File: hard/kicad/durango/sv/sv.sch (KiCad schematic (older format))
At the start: 22 parts, among them U1 74HCT02, U10 74HC245, U11 74HCT374, U12 74HC245, U13 74HC257, U15 74HC257, U16 74HC257, U17 74HC257, U18 74HC257, U2 74HCT4040, U3 74HC21, U4 74HCT4040, U5 74HC21, U6 74HCT85, U7 74HCT85, U8 74HCT85, U9 74HC175, X1 ACO-18.432MHz

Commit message: trying buses on durango kicad schematics
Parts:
- added U14: 6264, Package_DIP:DIP-28_W15.24mm, symbol Memory_RAM:6264
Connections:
- net VD7: now reaches U12.11 (B7)
- net VD7: now also U11.18 (D7), U14.19 (D7)
- net VD6: now reaches U12.12 (B6)
- net VD6: now also U11.17 (D6), U14.18 (D6)
- net VD5: now reaches U12.13 (B5)
- net VD5: now also U11.14 (D5), U14.17 (D5)
- net VD4: now reaches U12.14 (B4)
- net VD4: now also U11.13 (D4), U14.16 (D4)
- net VD3: now reaches U12.15 (B3)
- net VD3: now also U11.8 (D3), U14.15 (D3)
- net VD2: now reaches U12.16 (B2)
- net VD2: now also U11.7 (D2), U14.13 (D2)
- net VD1: now reaches U12.17 (B1)
- net VD1: now also U11.4 (D1), U14.12 (D1)
- net VD0: now reaches U12.18 (B0)
- net VD0: now also U11.3 (D0), U14.11 (D0)
- net \SEL renamed ~SEL
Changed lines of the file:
@@
 Connection ~ 800  7700
 Text GLabel 700  7700 0    50   Input ~ 0
-\SEL
+~SEL
 Wire Wire Line
 	7150 3500 7200 3500
@@
 Wire Wire Line
 	10100 5500 10050 5500
+$Comp
+L Memory_RAM:6264 U14
+U 1 1 606818EE
+P 6600 5400
+F 0 "U14" H 6600 6581 50  0000 C CNN
+F 1 "6264" H 6600 6490 50  0000 C CNN
+F 2 "Package_DIP:DIP-28_W15.24mm" H 6600 5400 50  0001 C CNN
+F 3 "http://users.ece.utexas.edu/~valvano/Datasheets/MCM6264.pdf" H 6600 5400 50  0001 C CNN
+	1    6600 5400
+	1    0    0    -1
+$EndComp
+Wire Bus Line
+	8750 4350 7300 4350
+Entry Wire Line
+	8750 5200 8850 5300
+Entry Wire Line
+	8750 5100 8850 5200
+Entry Wire Line
+	8750 5000 8850 5100
+Entry Wire Line
+	8750 4900 8850 5000
+Entry Wire Line
+	8750 4800 8850 4900
+Entry Wire Line
+	8750 4700 8850 4800
+Entry Wire Line
+	8750 4600 8850 4700
+Entry Wire Line
+	8750 4500 8850 4600
+Entry Wire Line
+	7200 5300 7300 5400
+Entry Wire Line
+	7200 5200 7300 5300
+Entry Wire Line
+	7200 5100 7300 5200
+Entry Wire Line
+	7200 5000 7300 5100
+Entry Wire Line
+	7200 4900 7300 5000
+Entry Wire Line
+	7200 4800 7300 4900
+Entry Wire Line
+	7200 4700 7300 4800
+Entry Wire Line
+	7200 4600 7300 4700
+Wire Wire Line
+	8850 5300 9050 5300
+Wire Wire Line
+	8850 5200 9050 5200
+Wire Wire Line
+	8850 5100 9050 5100
+Wire Wire Line
+	8850 5000 9050 5000
+Wire Wire Line
+	8850 4900 9050 4900
+Wire Wire Line
+	8850 4800 9050 4800
+Wire Wire Line
+	8850 4700 9050 4700
+Wire Wire Line
+	8850 4600 9050 4600
+Wire Wire Line
+	7000 5300 7200 5300
+Wire Wire Line
+	7000 5200 7200 5200
+Wire Wire Line
+	7000 5100 7200 5100
+Wire Wire Line
+	7000 5000 7200 5000
+Wire Wire Line
+	7000 4900 7200 4900
+Wire Wire Line
+	7000 4800 7200 4800
+Wire Wire Line
+	7000 4700 7200 4700
+Wire Wire Line
+	7000 4600 7200 4600
+Text Label 8900 5300 0    50   ~ 0
+VD7
+Text Label 8900 5200 0    50   ~ 0
+VD6
+Text Label 8900 5100 0    50   ~ 0
+VD5
+Text Label 8900 5000 0    50   ~ 0
+VD4
+Text Label 8900 4900 0    50   ~ 0
+VD3
+Text Label 8900 4800 0    50   ~ 0
+VD2
+Text Label 8900 4700 0    50   ~ 0
+VD1
+Text Label 8900 4600 0    50   ~ 0
+VD0
+Text Label 7050 5300 0    50   ~ 0
+VD7
+Text Label 7050 5200 0    50   ~ 0
+VD6
+Text Label 7050 5100 0    50   ~ 0
+VD5
+Text Label 7050 5000 0    50   ~ 0
+VD4
+Text Label 7050 4900 0    50   ~ 0
+VD3
+Text Label 7050 4800 0    50   ~ 0
+VD2
+Text Label 7050 4700 0    50   ~ 0
+VD1
+Text Label 7050 4600 0    50   ~ 0
+VD0
+Wire Bus Line
+	7300 4350 5750 4350
+Connection ~ 7300 4350
+Entry Wire Line
+	5750 2700 5850 2800
+Entry Wire Line
+	5750 2800 5850 2900
+Entry Wire Line
+	5750 2900 5850 3000
+Entry Wire Line
+	5750 3000 5850 3100
+Entry Wire Line
+	5750 3100 5850 3200
+Entry Wire Line
+	5750 3200 5850 3300
+Entry Wire Line
+	5750 3300 5850 3400
+Entry Wire Line
+	5750 3400 5850 3500
+Wire Wire Line
+	5850 2800 6150 2800
+Wire Wire Line
+	5850 2900 6150 2900
+Wire Wire Line
+	5850 3000 6150 3000
+Wire Wire Line
+	5850 3100 6150 3100
+Wire Wire Line
+	5850 3200 6150 3200
+Wire Wire Line
+	5850 3300 6150 3300
+Wire Wire Line
+	5850 3400 6150 3400
+Wire Wire Line
+	5850 3500 6150 3500
+Wire Bus Line
+	5750 2700 5750 4350
+Wire Bus Line
+	7300 4350 7300 5400
+Wire Bus Line
+	8750 4350 8750 5300
+Text Label 5900 2800 0    50   ~ 0
+VD0
+Text Label 5900 2900 0    50   ~ 0
+VD1
+Text Label 5900 3000 0    50   ~ 0
+VD2
+Text Label 5900 3100 0    50   ~ 0
+VD3
+Text Label 5900 3200 0    50   ~ 0
+VD4
+Text Label 5900 3300 0    50   ~ 0
+VD5
+Text Label 5900 3400 0    50   ~ 0
+VD6
+Text Label 5900 3500 0    50   ~ 0
+VD7
 $EndSCHEMATC

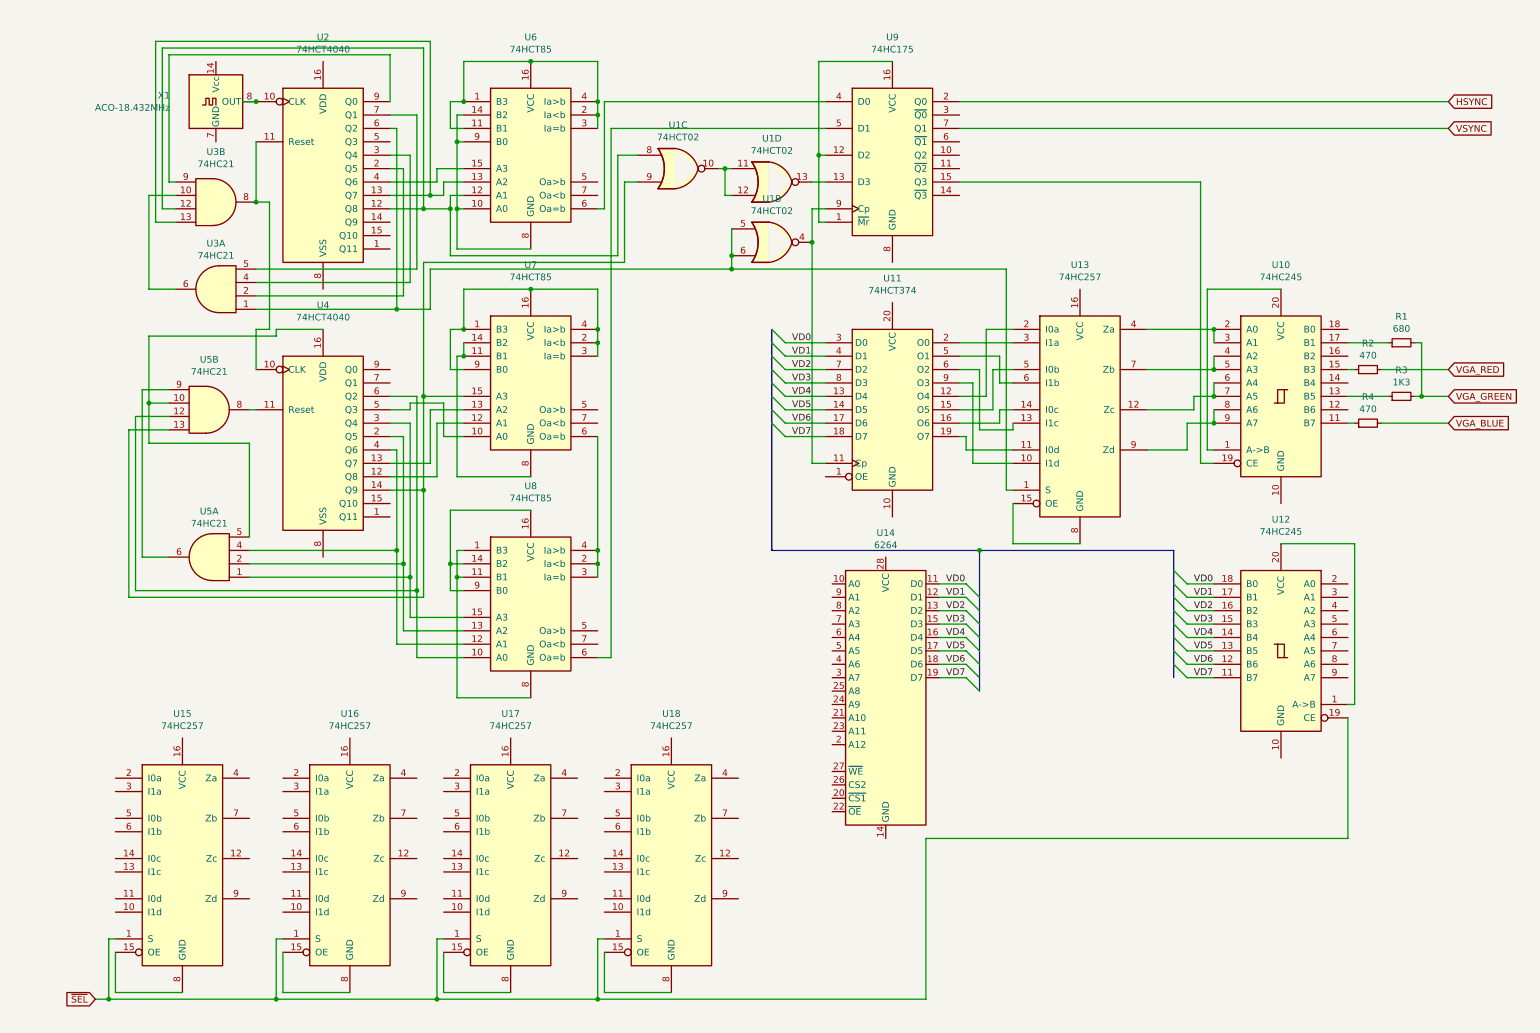
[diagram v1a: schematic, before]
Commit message: finished durango-sv schematic
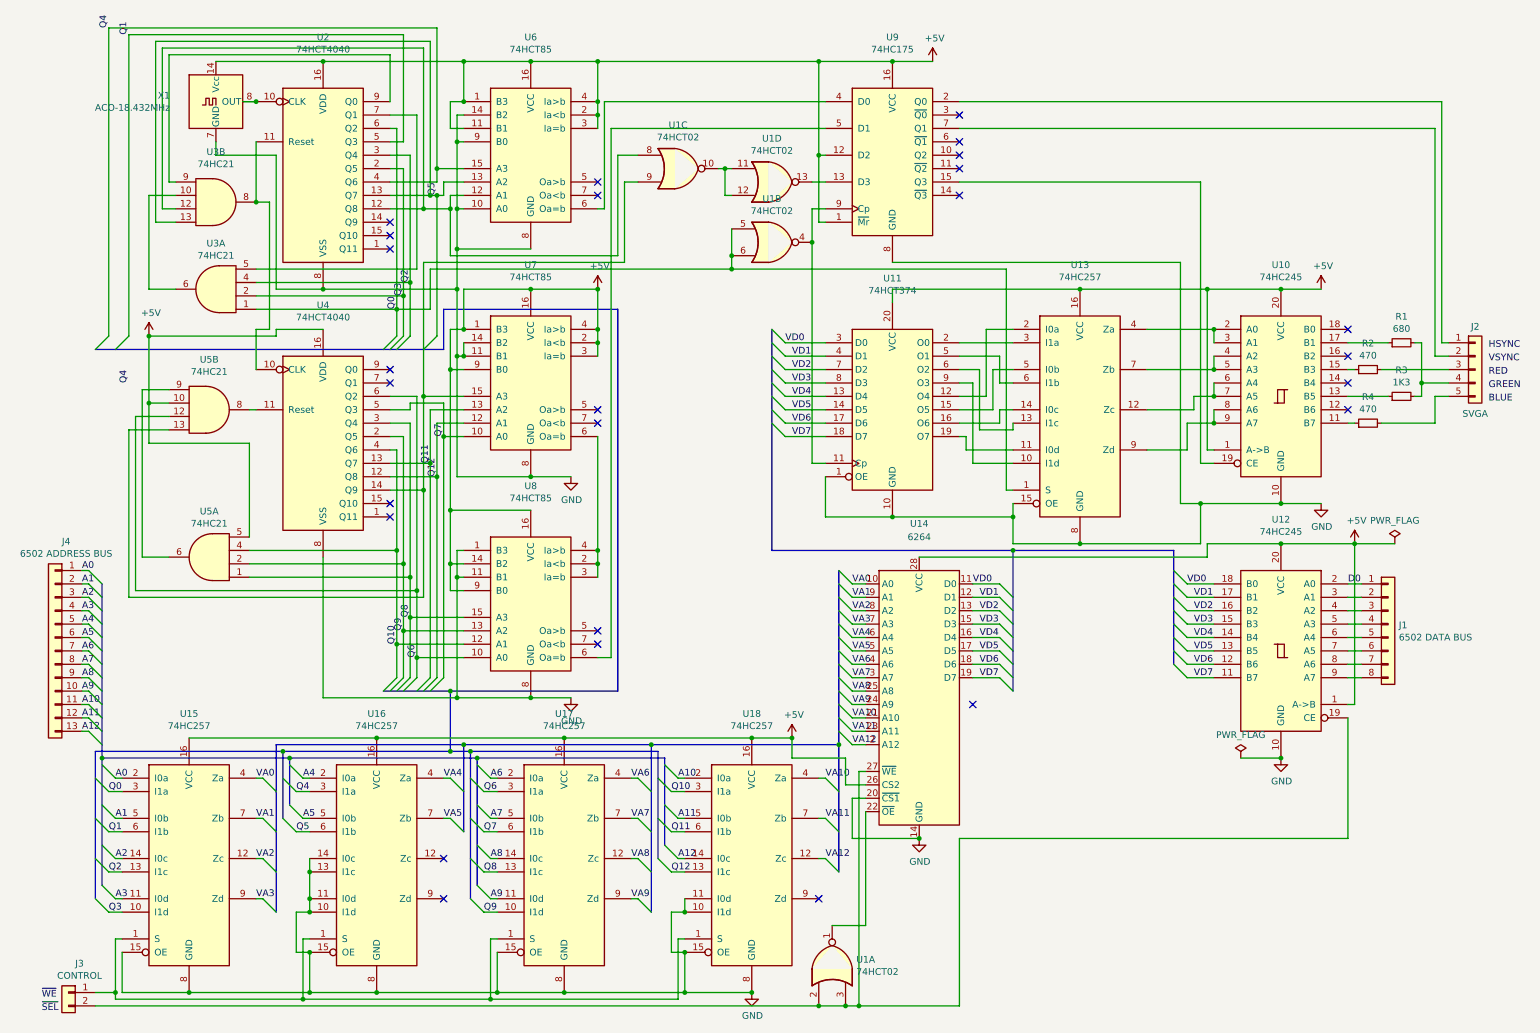
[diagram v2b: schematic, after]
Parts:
- added J1: 6502 DATA BUS, symbol Connector_Generic:Conn_01x08
- added J2: SVGA, symbol Connector_Generic:Conn_01x05
- added J3: CONTROL, symbol Connector_Generic:Conn_01x02
- added J4: 6502 ADDRESS BUS, symbol Connector_Generic:Conn_01x13
- added unit 1 of U1
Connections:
- net HSYNC: no longer U9.2 (Q0)
- net VSYNC: no longer U9.7 (Q1)
- net ~SEL: no longer U12.19 (CE), U15.1 (S), U16.1 (S), U17.1 (S), U18.1 (S)
- net +5V: now reaches X1.14 (Vcc)
- net +5V: now also U10.1 (A->B), U10.20 (VCC), U11.20 (VCC), U12.1 (A->B), U12.20 (VCC), U13.16 (VCC), U14.26 (CS2), U14.28 (VCC), U15.16 (VCC), U16.16 (VCC), U17.16 (VCC), U18.16 (VCC), U2.16 (VDD), U4.16 (VDD), U5.10, U5.5, U6.1 (B3), U6.11 (B1), U6.16 (VCC), U6.2 (Ia<b), U6.3 (Ia=b), U6.4 (Ia>b), U7.1 (B3), U7.16 (VCC), U7.2 (Ia<b), U7.3 (Ia=b), U7.4 (Ia>b), U7.9 (B0), U8.14 (B2), U8.16 (VCC), U8.9 (B0), U9.1 (~Mr), U9.12 (D2), U9.16 (VCC)
- net GND: now reaches X1.7 (GND)
- net GND: now also U10.10 (GND), U11.1 (OE), U11.10 (GND), U12.10 (GND), U13.15 (OE), U13.8 (GND), U14.14 (GND), U14.20 (~CS1), U15.15 (OE), U15.8 (GND), U16.10 (I1d), U16.11 (I0d), U16.13 (I1c), U16.14 (I0c), U16.15 (OE), U16.8 (GND), U17.15 (OE), U17.8 (GND), U18.10 (I1d), U18.11 (I0d), U18.15 (OE), U18.8 (GND), U2.8 (VSS), U4.8 (VSS), U6.10 (A0), U6.14 (B2), U6.8 (GND), U6.9 (B0), U7.11 (B1), U7.14 (B2), U7.8 (GND), U8.1 (B3), U8.11 (B1), U8.8 (GND), U9.8 (GND)
- net Q5: now reaches U2.13 (Q7), U3.13, U6.13 (A2)
- net Q5: now also U16.6 (I1b)
- net Q3: now reaches U2.2 (Q5), U3.2
- net Q3: now also U15.10 (I1d)
- net Q2: now reaches U2.3 (Q4), U3.4
- net Q2: now also U15.13 (I1c)
- net Q4: now reaches U2.4 (Q6), U6.15 (A3)
- net Q4: now also U16.3 (I1a)
- net Q1: now reaches U2.5 (Q3)
- net Q1: now also U15.6 (I1b)
- net Q0: now reaches U1.5, U1.6, U13.1 (S), U2.6 (Q2), U3.1
- net Q0: now also U15.3 (I1a)
- net Q12: now reaches U4.12 (Q8), U7.12 (A1)
- net Q12: now also U18.13 (I1c)
- net Q11: now reaches U4.13 (Q7), U7.13 (A2)
- net Q11: now also U18.6 (I1b)
- net Q9: now reaches U4.2 (Q5), U5.2, U8.13 (A2)
- net Q9: now also U17.10 (I1d)
- net Q8: now reaches U4.3 (Q4), U5.1, U8.15 (A3)
- net Q8: now also U17.13 (I1c)
- net Q10: now reaches U4.4 (Q6), U5.4, U8.12 (A1)
- net Q10: now also U18.3 (I1a)
- net Q7: now reaches U4.5 (Q3), U7.10 (A0)
- net Q7: now also U17.6 (I1b)
- net Q6: now reaches U4.6 (Q2), U5.12, U8.10 (A0)
- net Q6: now also U17.3 (I1a)
- net VA0: now reaches U14.10 (A0)
- net VA0: now also U15.4 (Za)
- net VA12: now reaches U14.2 (A12)
- net VA12: now also U18.12 (Zc)
- net VA10: now reaches U14.21 (A10)
- net VA10: now also U18.4 (Za)
- net at U14.22 (~OE): now also U1.1
- net VA11: now reaches U14.23 (A11)
- net VA11: now also U18.7 (Zb)
- net VA9: now reaches U14.24 (A9)
- net VA9: now also U17.9 (Zd)
- net VA8: now reaches U14.25 (A8)
- net VA8: now also U17.12 (Zc)
- net at U14.27 (~WE): now also U12.19 (CE), J3.2 (Pin_2), U1.2, U1.3
- net VA7: now reaches U14.3 (A7)
- net VA7: now also U17.7 (Zb)
- net VA6: now reaches U14.4 (A6)
- net VA6: now also U17.4 (Za)
- net VA5: now reaches U14.5 (A5)
- net VA5: now also U16.7 (Zb)
- net VA4: now reaches U14.6 (A4)
- net VA4: now also U16.4 (Za)
- net VA3: now reaches U14.7 (A3)
- net VA3: now also U15.9 (Zd)
- net VA2: now reaches U14.8 (A2)
- net VA2: now also U15.12 (Zc)
- net VA1: now reaches U14.9 (A1)
- net VA1: now also U15.7 (Zb)
- net D0: now reaches U12.2 (A0)
- net D0: now also J1.1 (Pin_1)
- net at U12.3 (A1): now also J1.2 (Pin_2)
- net at U12.4 (A2): now also J1.3 (Pin_3)
- net at U12.5 (A3): now also J1.4 (Pin_4)
- net at U12.6 (A4): now also J1.5 (Pin_5)
- net at U12.7 (A5): now also J1.6 (Pin_6)
- net at U12.8 (A6): now also J1.7 (Pin_7)
- net at U12.9 (A7): now also J1.8 (Pin_8)
- net A9: now reaches U17.11 (I0d)
- net A9: now also J4.10 (Pin_10)
- net A8: now reaches U17.14 (I0c)
- net A8: now also J4.9 (Pin_9)
- net A6: now reaches U17.2 (I0a)
- net A6: now also J4.7 (Pin_7)
- net A7: now reaches U17.5 (I0b)
- net A7: now also J4.8 (Pin_8)
- net A4: now reaches U16.2 (I0a)
- net A4: now also J4.5 (Pin_5)
- net A5: now reaches U16.5 (I0b)
- net A5: now also J4.6 (Pin_6)
- net A3: now reaches U15.11 (I0d)
- net A3: now also J4.4 (Pin_4)
- net A2: now reaches U15.14 (I0c)
- net A2: now also J4.3 (Pin_3)
- net A0: now reaches U15.2 (I0a)
- net A0: now also J4.1 (Pin_1)
- net A1: now reaches U15.5 (I0b)
- net A1: now also J4.2 (Pin_2)
- net A12: now reaches U18.14 (I0c)
- net A12: now also J4.13 (Pin_13)
- net A10: now reaches U18.2 (I0a)
- net A10: now also J4.11 (Pin_11)
- net A11: now reaches U18.5 (I0b)
- net A11: now also J4.12 (Pin_12)
- net VGA_BLUE: no longer names the net of R4.2
- net VGA_BLUE: now also J2.5 (Pin_5)
- net VGA_GREEN: no longer names the net of R1.2, R3.2
- net VGA_GREEN: now also J2.4 (Pin_4)
- net VGA_RED: no longer names the net of R2.2
- net VGA_RED: now also J2.3 (Pin_3)
- new net: J2.1 (Pin_1), U9.2 (Q0)
- new net: J2.2 (Pin_2), U9.7 (Q1)
- new net: J3.1 (Pin_1), U15.1 (S), U16.1 (S), U17.1 (S), U18.1 (S)
- no-connect marks 0 -> 26
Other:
- moved on the sheet: U14, U15, U16, U17, U18

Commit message: some fixes on Durango-SV schematic
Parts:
- U11: symbol 74xx:74HC374 -> 74xx:74LS374
- U14: symbol Memory_RAM:6264 -> 6264:6264
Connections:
- net BLUE: now also J2.5 (Pin_5), R4.1
- net GND: no longer U11.10 (GND)
- net GREEN: now also J2.4 (Pin_4), R1.2, R3.2
- net HSYNC: now also J2.1 (Pin_1), U9.2 (Q0)
- net RED: now also J2.3 (Pin_3), R2.2
- net VSYNC: now also J2.2 (Pin_2), U9.7 (Q1)
- net ~SEL: now also J3.1 (Pin_1), U15.1 (S), U16.1 (S), U17.1 (S), U18.1 (S)
- net ~WE: now also J3.2 (Pin_2), U1.2, U1.3, U12.19 (CE), U14.27 (~WE)
- net at U10.11 (B7): now also R4.2; no longer R4.1
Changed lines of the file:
@@
 EESchema Schematic File Version 4
-LIBS:power
-LIBS:74xx
 LIBS:sv-cache
-EELAYER 30 0
+EELAYER 29 0
 EELAYER END
 $Descr A4 11693 8268
@@
 $EndComp
 $Comp
-L 74xx:74HC374 U11
+L 74xx:74LS374 U11
 U 1 1 6075F5C4
 P 6650 3300
@@
 F 3 "~" H 10200 3400 50  0001 C CNN
 	1    10200 3400
-	0    -1   -1   0
+	0    1    1    0
 $EndComp
 Wire Wire Line
@@
 	1600 1400 1600 1300
 Connection ~ 2400 2400
-Wire Wire Line
-	6650 4100 7550 4100
 Connection ~ 7550 4100
 Wire Wire Line
@@
 $EndComp
 Connection ~ 4450 2400
-Text Label 7250 4600 0    50   ~ 0
+Text Label 7300 4600 0    50   ~ 0
 VD0
-Text Label 8850 4600 0    50   ~ 0
+Text Label 8900 4600 0    50   ~ 0
 VD0
-Text Label 5850 2800 0    50   ~ 0
+Text Label 5900 2800 0    50   ~ 0
 VD0
 $Comp
-L Memory_RAM:6264 U14
+L 6264:6264 U14
 U 1 1 606818EE
 P 6850 5400
@@
 Text Label 800  450  1    50   ~ 0
 Q4
-Connection ~ 6850 6500
 Wire Wire Line
 	5900 5750 5900 5900
@@
 Wire Wire Line
 	6150 3800 6150 4100
-Wire Wire Line
-	6150 4100 6650 4100
-Connection ~ 6650 4100
 $Comp
 L Connector_Generic:Conn_01x08 J1
@@
 Text Label 10050 4600 0    50   ~ 0
 D0
-Text Label 11100 2850 0    50   ~ 0
+Text Label 10750 2650 0    50   ~ 0
 HSYNC
-Text Label 11100 2950 0    50   ~ 0
+Text Label 10700 2900 1    50   ~ 0
 VSYNC
-Text Label 11100 3050 0    50   ~ 0
+Text Label 10650 3000 0    50   ~ 0
 RED
-Text Label 11100 3150 0    50   ~ 0
+Text Label 10600 3100 0    50   ~ 0
 GREEN
-Text Label 11100 3250 0    50   ~ 0
+Text Label 10700 3400 0    50   ~ 0
 BLUE
 Wire Wire Line
@@
 	-1   0    0    -1
 $EndComp
-Text Label 300  7700 0    50   ~ 0
+Text Label 700  7750 0    50   ~ 0
 ~WE
-Text Label 300  7800 0    50   ~ 0
+Text Label 700  7650 0    50   ~ 0
 ~SEL
 $Comp
@@
 Wire Wire Line
 	7150 6500 7150 7750
+Connection ~ 6400 7750
+Wire Wire Line
+	6150 4100 7550 4100
 Wire Wire Line
 	3150 2200 3150 3200
@@
 Wire Bus Line
 	750  4600 750  5900
-Connection ~ 6400 7750
 $EndSCHEMATC
